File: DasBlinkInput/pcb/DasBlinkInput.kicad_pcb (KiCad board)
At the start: 4 copper layers, 60 x 16 mm, 35 parts, among them P101 CONN_01X02, P102 TP_VGND, P103 TP_GND, P104 TP_3V, P105 CONN_01X05, P106 VREF, P201 TP_CHAN1, P301 TP_CHAN2, P401 TP_CHAN3, P501 TP_CHAN4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

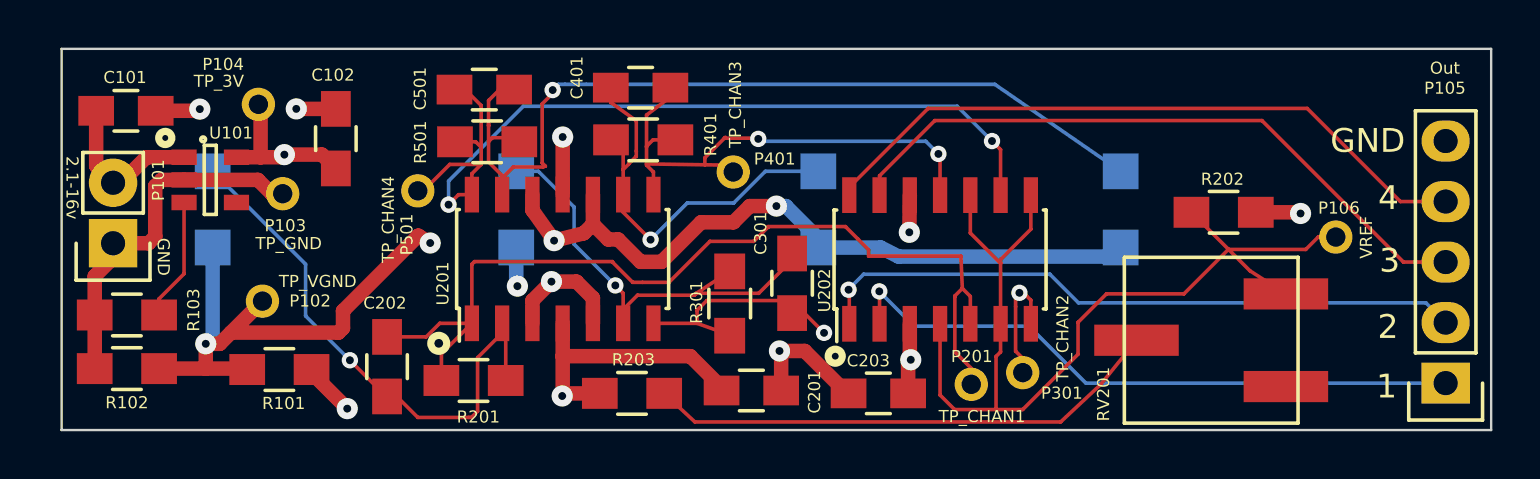
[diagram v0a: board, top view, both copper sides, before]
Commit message: DBI - fixed reg/on pin, changed resistor to 0 ohm near divider and rv, added 10k pull up resistors to 3V for each output channel.
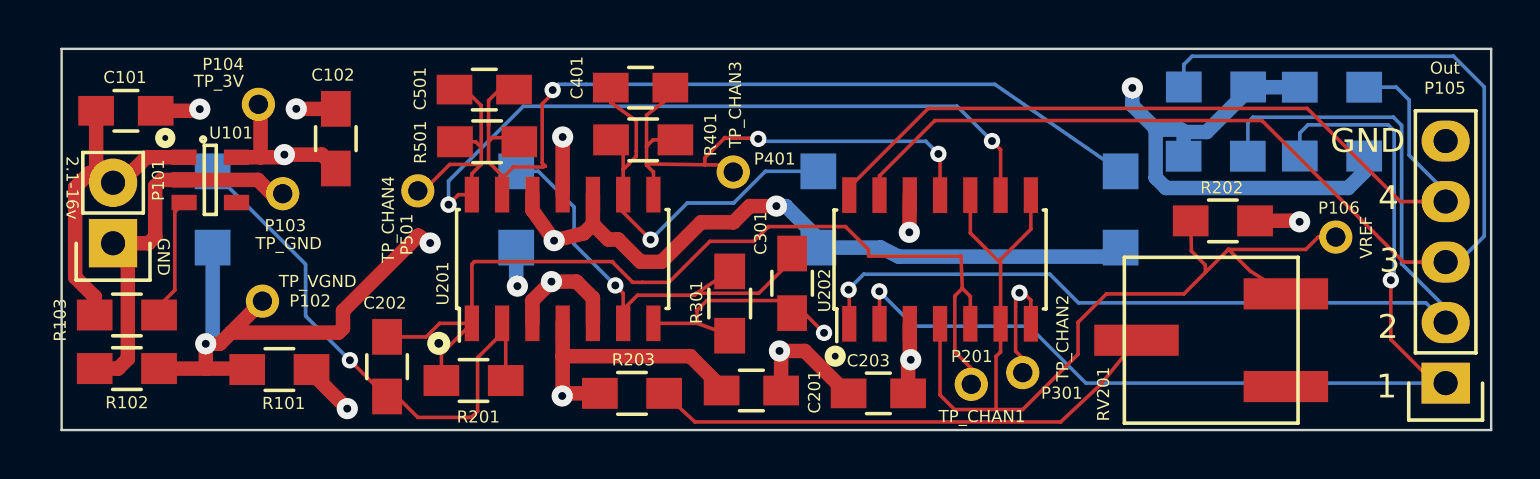
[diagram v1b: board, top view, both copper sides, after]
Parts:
- added R204: 10K, Resistors_SMD:R_0805_HandSoldering, B.Cu at (143.3, 88.5)
- added R302: 10K, Resistors_SMD:R_0805_HandSoldering, B.Cu at (138.4, 88.5)
- added R402: 10K, Resistors_SMD:R_0805_HandSoldering, B.Cu at (138.4, 85.6)
- added R502: 10K, Resistors_SMD:R_0805_HandSoldering, B.Cu at (143.3, 85.6)
- R203: value 10K -> 0
- moved R202 0.36 mm to (138.7, 91.2)
- turned R103 to 0 degrees
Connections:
- R103 pad 1: Net-(R103-Pad1) -> Net-(C101-Pad1)
- R103 pad 2: GND -> Net-(R103-Pad2)
- U101 pad 3: Net-(R103-Pad1) -> Net-(R103-Pad2)
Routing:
- net /Channel3Photodetect/CHAN3_OUT: track 28.0 -> 50.8 mm
- net 3V: track 24.0 -> 46.2 mm, vias 4 -> 5
- net /Channel2Photodetect/CHAN2_OUT: track 27.6 -> 45.3 mm
- net /Channel1Photodetect/CHAN1_OUT: track 26.7 -> 44.3 mm, vias 1 -> 2
- net Net-(C101-Pad1): track 6.74 -> 14.4 mm
- net /Channel4Photodetect/CHAN4_OUT: track 28.4 -> 35.6 mm
- net Net-(R103-Pad1): track 5.15 -> 0.00 mm
- net Net-(R103-Pad2): track 0.00 -> 5.15 mm
- net GND: track 30.1 -> 31.7 mm
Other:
- board text added: "DasBlinkInput : dbi_v2"
- board text removed: "DasBlinkInput : dbi_v1"
